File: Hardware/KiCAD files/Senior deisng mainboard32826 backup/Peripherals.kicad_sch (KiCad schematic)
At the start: 39 parts, among them J43 USB, Q13 BSS138, Q20 BC807, SW1 SPDT_Slide_PTH_11.6x4.0mm, SW2 SPDT_Slide_PTH_11.6x4.0mm, SW3 SPDT_Slide_PTH_11.6x4.0mm, SW4 SPDT_Slide_PTH_11.6x4.0mm, U20 RClamp0504FB, U22 AP22816AKEWT

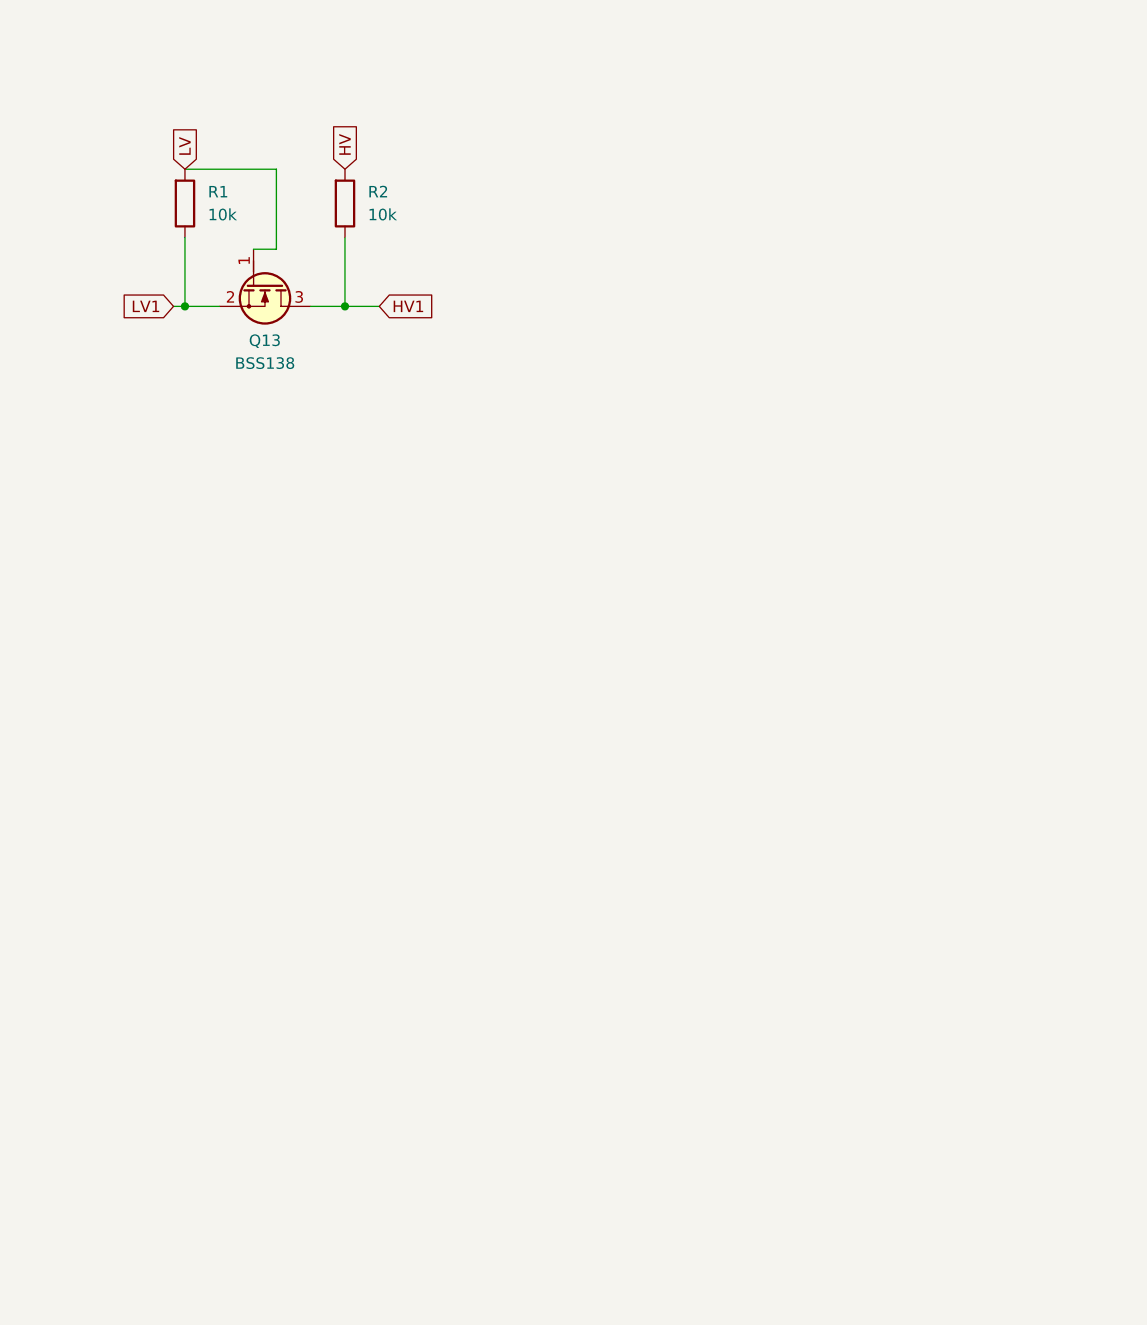
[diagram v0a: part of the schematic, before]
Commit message: added more schematics for initial design
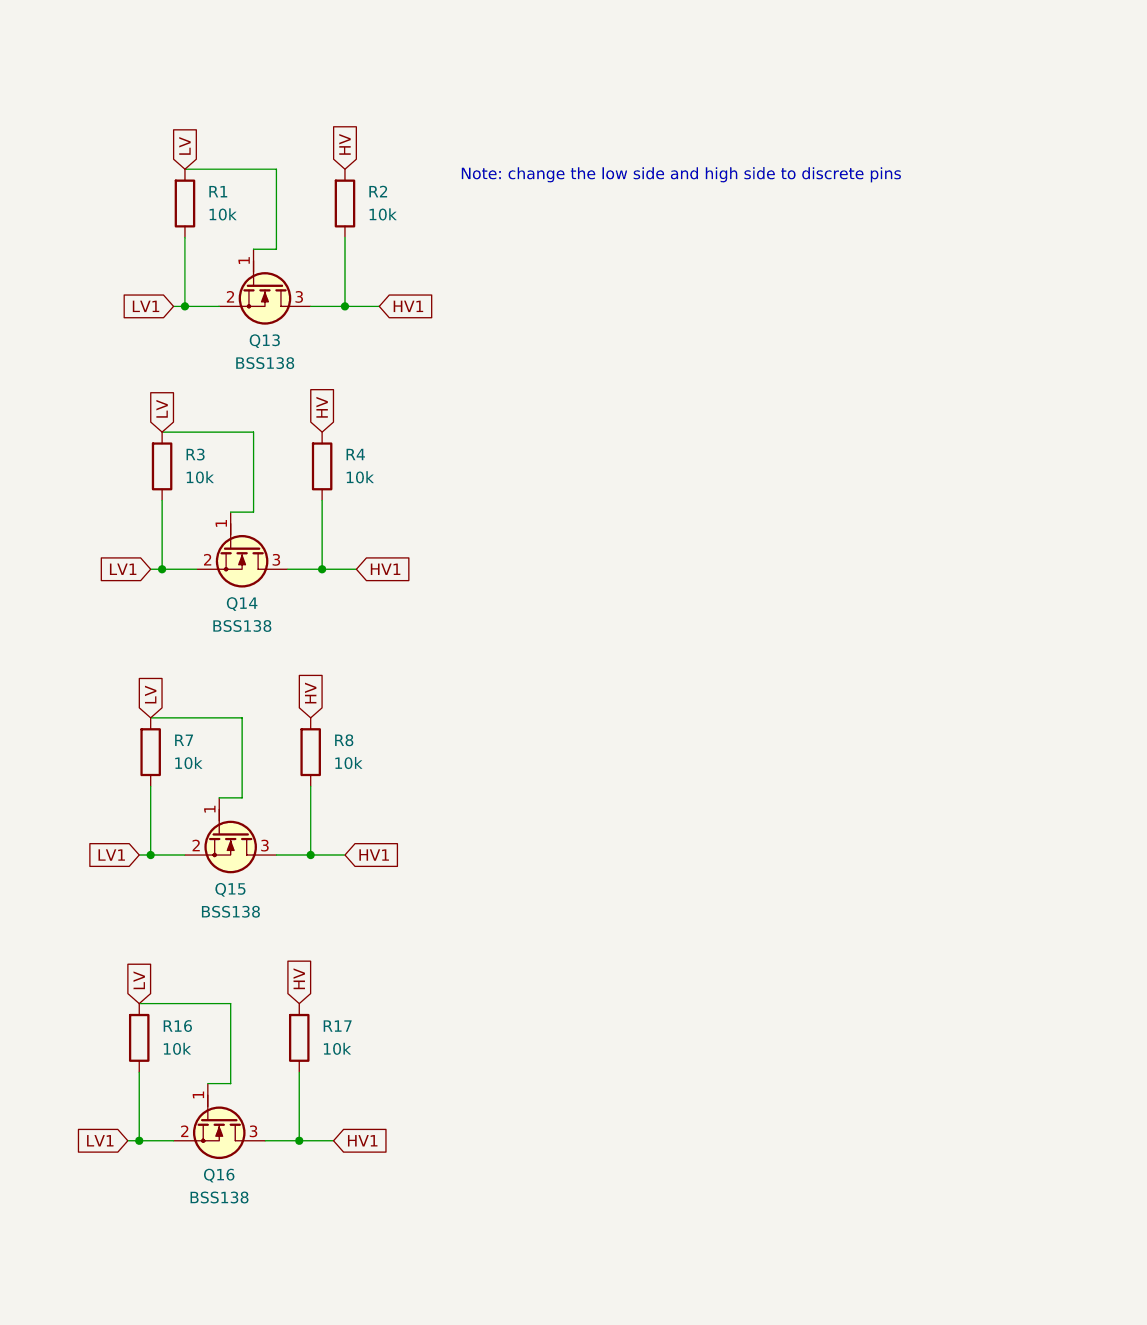
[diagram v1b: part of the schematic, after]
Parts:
- added Q14, Q15, Q16: BSS138, PCM_Package_TO_SOT_SMD_AKL:SOT-23, symbol PCM_Transistor_MOSFET_AKL:BSS138
- added R16, R17, R3, R4, R7, R8: 10k, symbol PCM_Resistor_AKL:R_Generic
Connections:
- net HV: now also R17.1, R4.1, R8.1
- net HV1: now also Q14.3 (D), Q15.3 (D), Q16.3 (D), R17.2, R4.2, R8.2
- net LV: now also Q14.1 (G), Q15.1 (G), Q16.1 (G), R16.1, R3.1, R7.1
- net LV1: now also Q14.2 (S), Q15.2 (S), Q16.2 (S), R16.2, R3.2, R7.2
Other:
- note added: "Note: change the low side and high side to discrete pins"

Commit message: Schematic adjustments made prior to initial submission to Chan thursday
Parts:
- added U5: TFT_320x240, z_Devices:TFT-320x240, symbol ILI9341 TFT screen:TFT_320x240
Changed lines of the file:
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@@
+	)
+	(symbol
+		(lib_id "ILI9341 TFT screen:TFT_320x240")
+		(at 511.81 163.83 0)
+		(unit 1)
+		(body_style 1)
+		(exclude_from_sim no)
+		(in_bom yes)
+		(on_board yes)
+		(in_pos_files yes)
+		(dnp no)
+		(fields_autoplaced yes)
+		(property "Reference" "U5"
+			(at 532.13 138.4299 0)
+			(show_name no)
+			(do_not_autoplace no)
+			(effects
+				(font
+					(size 1.27 1.27)
+				)
+				(justify left)
+			)
+		)
+		(property "Value" "TFT_320x240"
+			(at 532.13 140.9699 0)
+			(show_name no)
+			(do_not_autoplace no)
+			(effects
+				(font
+					(size 1.27 1.27)
+				)
+				(justify left)
+			)
+		)
+		(property "Footprint" "z_Devices:TFT-320x240"
+			(at 532.13 143.5099 0)
+			(show_name no)
+			(do_not_autoplace no)
+			(effects
+				(font
+					(size 1.27 1.27)
+				)
+				(justify left)
+			)
+		)
+		(property "Datasheet" ""
+			(at 720.09 141.605 0)
+			(hide yes)
+			(show_name no)
+			(do_not_autoplace no)
+			(effects
+				(font
+					(size 1.27 1.27)
+				)
+			)
+		)
+		(property "Description" ""
+			(at 511.81 163.83 0)
+			(hide yes)
+			(show_name no)
+			(do_not_autoplace no)
+			(effects
+				(font
+					(size 1.27 1.27)
+				)
+			)
+		)
+		(pin "13"
+		)
+		(pin "14"
+		)
+		(pin "5"
+		)
+		(pin "3"
+		)
+		(pin "7"
+		)
+		(pin "6"
+		)
+		(pin "8"
+		)
+		(pin "12"
+		)
+		(pin "1"
+		)
+		(pin "2"
+		)
+		(pin "11"
+		)
+		(pin "4"
+		)
+		(pin "9"
+		)
+		(pin "10"
+		)
+		(instances
+			(project "Senior design Mainboard"
+				(path "/1027da72-a2dd-4309-b004-99ab5e04adbe/9095e8d5-0d3d-4f63-98f2-4261bdd8f9fe"
+					(reference "U5")
+					(unit 1)
+				)
+			)
+		)
 	)
 	(symbol

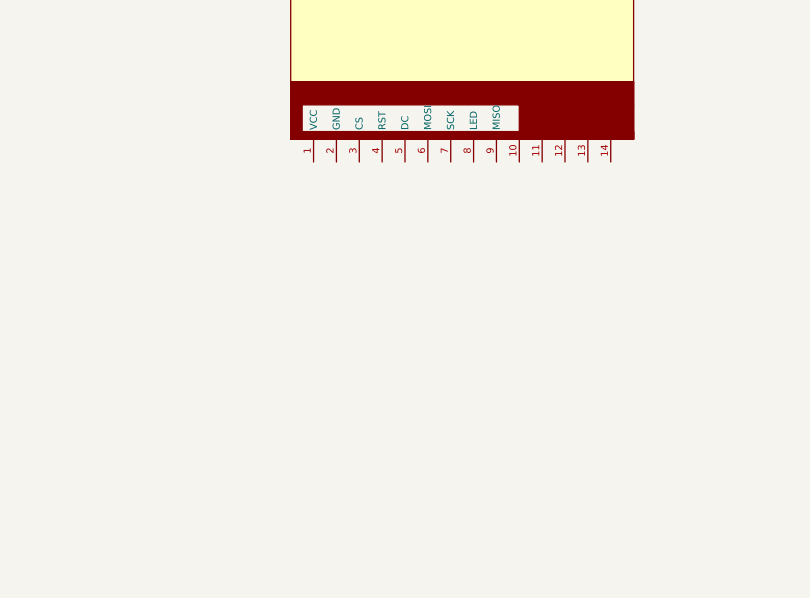
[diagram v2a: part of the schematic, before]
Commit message: MCU power, new MCU placed, LCD communication, AC coupling of voltage reg on MCU
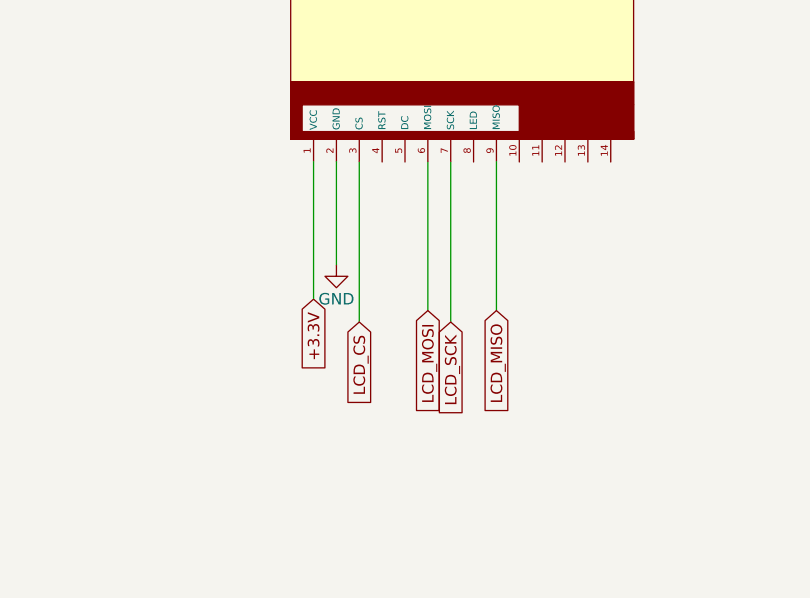
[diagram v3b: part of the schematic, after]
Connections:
- net +3.3V: now also U5.1 (VCC)
- net GND: now also U5.2 (GND)
- net LCD_CS: now reaches U5.3 (CS)
- net LCD_MOSI: now reaches U5.6 (MOSI)
- net LCD_SCK: now reaches U5.7 (SCK)
- net LCD_MISO: now reaches U5.9 (MISO)

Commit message: IO pull resistors, Motor driver V1, LCD communication
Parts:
- removed Q13, Q14, Q15, Q16: BSS138, PCM_Package_TO_SOT_SMD_AKL:SOT-23, symbol PCM_Transistor_MOSFET_AKL:BSS138
- removed R1, R16, R17, R2, R3, R4, R7, R8: 10k, symbol PCM_Resistor_AKL:R_Generic
- added ILI9341_LCD1: (no value), symbol FUNNY_TFT symbol:ILI9341_TFT
- added J10, J9: Conn_01x02, PCM_SparkFun-Connector:1x02_P2.54mm, symbol PCM_SparkFun-Connector:Conn_01x02_P2.54mm
- added J5, J6, J7: JST_1mm_3_Vertical, PCM_SparkFun-Connector:JST_1x03_P1.0mm_Vertical_SMD, symbol PCM_SparkFun-Connector:Conn_01x03_JST_P1.0mm_Vertical_SMD
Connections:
- net +3.3V: now also SW1.2 (B), SW2.2 (B), SW3.2 (B), SW4.2 (B), ILI9341_LCD1.1 (VCC), ILI9341_LCD1.8 (LED), J10.2 (Pin_2), J6.1, J7.1, J9.2 (Pin_2); no longer U5.1 (VCC)
- net GND: now also ILI9341_LCD1.2 (GND), J10.1 (Pin_1), J6.2, J7.2, J9.1 (Pin_1); no longer U5.2 (GND)
- net LCD_CS: now also ILI9341_LCD1.3 (CS); no longer U5.3 (CS)
- net LCD_MISO: now also ILI9341_LCD1.9 (SDO(MISO)); no longer U5.9 (MISO)
- net LCD_MOSI: now also ILI9341_LCD1.6 (SDI(MOSI)); no longer U5.6 (MOSI)
- net LCD_SCK: now also ILI9341_LCD1.7 (SCK); no longer U5.7 (SCK)
- net AXIS_X_ENDSTOP: now reaches SW1.3 (C)
- net AXIS_X_ENDSTOP: now also SW2.3 (C), SW3.3 (C), SW4.3 (C)
- new net LCD_RESET: ILI9341_LCD1.4 (RESET)
- new net TFT_CLK: ILI9341_LCD1.10 (T_clk)
- new net TFT_CS: ILI9341_LCD1.11 (T_CS)
- new net TFT_IN: ILI9341_LCD1.12 (T_DIN)
- new net TFT_INTERRUPT: ILI9341_LCD1.14 (T_IRQ)
- new net TFT_OUT: ILI9341_LCD1.13 (T_DO)
- no-connect marks 2 -> 10
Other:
- note added: "check if interrupt is bidirectional"
- note added: "confirm fan wiring and connector on ender3"
- note added: "hotplate peripheral connections"
- note removed: "Note: change the low side and high side to discrete pins"

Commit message: 1.1, devices have been cleaned up
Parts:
- removed J10, J9: Conn_01x02, PCM_SparkFun-Connector:1x02_P2.54mm, symbol PCM_SparkFun-Connector:Conn_01x02_P2.54mm
- removed J5: JST_1mm_3_Vertical, PCM_SparkFun-Connector:JST_1x03_P1.0mm_Vertical_SMD, symbol PCM_SparkFun-Connector:Conn_01x03_JST_P1.0mm_Vertical_SMD
- removed U5: TFT_320x240, z_Devices:TFT-320x240, symbol ILI9341 TFT screen:TFT_320x240
- added J3: Conn_01x02, PCM_SparkFun-Connector:1x02_P2.54mm, symbol PCM_SparkFun-Connector:Conn_01x02_P2.54mm
- added SW7: SPDT_Slide_PTH_11.6x4.0mm, PCM_SparkFun-Switch:Slide_SPDT_PTH_11.6x4.0mm, symbol PCM_SparkFun-Switch:SPDT_Slide_PTH_11.6x4.0mm
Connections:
- net LCD_CS is gone; now on net SPI4_CS: ILI9341_LCD1.3 (CS)
- net LCD_MISO is gone; now on net CHAINL0_MISO_4: ILI9341_LCD1.9 (SDO(MISO))
- net LCD_SCK is gone; now on net SPI4_SCK: ILI9341_LCD1.7 (SCK)
- net TFT_CLK is gone; now on net SPI4_SCK: ILI9341_LCD1.10 (T_clk)
- net TFT_CS is gone; now on net SPI4_CS: ILI9341_LCD1.11 (T_CS)
- net TFT_IN is gone; now on net CHAINL1_MISO_4: ILI9341_LCD1.12 (T_DIN)
- net +3.3V: now also SW7.2 (B)
- net AXIS_X_ENDSTOP: now also SW7.3 (C)
- net DATA_SELECT: now also ILI9341_LCD1.5 (D/C)
- net GND: now also J3.2 (Pin_2)
- net SPI4_SCK: now reaches ILI9341_LCD1.15 (SD_SCK)
- net CHAINL1_MISO_4: now reaches ILI9341_LCD1.16 (SD_MISO)
- net CHAINL0_MISO_4: now reaches ILI9341_LCD1.17 (SD_MOSI)
- net SPI4_CS: now reaches ILI9341_LCD1.18 (SD_CS)
- net LCD_MOSI renamed MOSI_4
- net TFT_OUT renamed MISO_4
- new net TEMP_HOTPLATE: J3.1 (Pin_1)
- no-connect marks 10 -> 9
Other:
- note added: "Check the speed of SPI here, in order to avoid jittering"
- note added: "SPI is 1110"
- note added: "to be swapped for USB-A"
- moved on the sheet: D63, D7, ILI9341_LCD1, J6, J7, R132, R21, SW1, SW2, SW3, SW4
